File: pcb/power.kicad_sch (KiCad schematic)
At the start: 38 parts, among them Q1 AO3407A, Q2 PMV20EN, Q3 NCE3401AY, Q4 NCE3401AY, Q5 DMMT5401, U2 MT1471

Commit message: Basic value changes
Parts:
- R10, R11: value 220R -> 3k3
- R6: value 680R -> 510R
- R7: value 1.5k -> 10k; footprint Resistor_SMD:R_0805_2012Metric -> Resistor_SMD:R_0402_1005Metric
- R9: value 12k -> 39k
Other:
- note added: "EN threshold is 1.8V"
- note removed: "EN threshold is 0.8V"
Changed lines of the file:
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@@
     (stroke (width 0) (type default) (color 0 0 0 0))
   )
-  (text "EN threshold is 0.8V" (at 93.218 83.566 0)
+  (text "EN threshold is 1.8V" (at 93.218 83.566 0)
     (effects (font (size 1.27 1.27)) (justify left bottom))
   )
@@
       (effects (font (size 1.27 1.27)) (justify left))
     )
-    (property "Value" "1.5k" (id 1) (at 49.53 154.1779 0)
-      (effects (font (size 1.27 1.27)) (justify left))
-    )
-    (property "Footprint" "Resistor_SMD:R_0805_2012Metric" (id 2) (at 45.72 152.908 90)
+    (property "Value" "10k" (id 1) (at 49.53 154.1779 0)
+      (effects (font (size 1.27 1.27)) (justify left))
+    )
+    (property "Footprint" "Resistor_SMD:R_0402_1005Metric" (id 2) (at 45.72 152.908 90)
       (effects (font (size 1.27 1.27)) hide)
     )
@@
   (symbol (lib_id "Device:R") (at 94.615 160.655 0) (unit 1)
     (in_bom yes) (on_board yes) (fields_autoplaced)
-    (property "Reference" "R10" (id 0) (at 97.155 159.3849 0)
-      (effects (font (size 1.27 1.27)) (justify left))
-    )
-    (property "Value" "220R" (id 1) (at 97.155 161.9249 0)
+    (property "Reference" "R10" (id 0) (at 96.52 159.3849 0)
+      (effects (font (size 1.27 1.27)) (justify left))
+    )
+    (property "Value" "3k3" (id 1) (at 96.52 161.9249 0)
       (effects (font (size 1.27 1.27)) (justify left))
     )
@@
       (effects (font (size 1.27 1.27)) (justify left))
     )
-    (property "Value" "220R" (id 1) (at 121.92 161.9249 0)
+    (property "Value" "3k3" (id 1) (at 121.92 161.9249 0)
       (effects (font (size 1.27 1.27)) (justify left))
     )
@@
       (effects (font (size 1.27 1.27)) (justify left))
     )
-    (property "Value" "12k" (id 1) (at 91.44 80.0099 0)
+    (property "Value" "39k" (id 1) (at 91.44 80.0099 0)
       (effects (font (size 1.27 1.27)) (justify left))
     )
@@
       (effects (font (size 1.27 1.27)) hide)
     )
-    (pin "1")
-    (pin "2")
-    (pin "6")
     (pin "3")
     (pin "4")
@@
       (effects (font (size 1.27 1.27)) (justify right))
     )
-    (property "Value" "680R" (id 1) (at 138.43 88.8999 0)
+    (property "Value" "510R" (id 1) (at 138.43 88.8999 0)
       (effects (font (size 1.27 1.27)) (justify right))
     )
@@
     (pin "2")
     (pin "6")
-    (pin "3")
-    (pin "4")
-    (pin "5")
   )
   (symbol (lib_id "Device:C") (at 177.165 66.04 0) (unit 1)

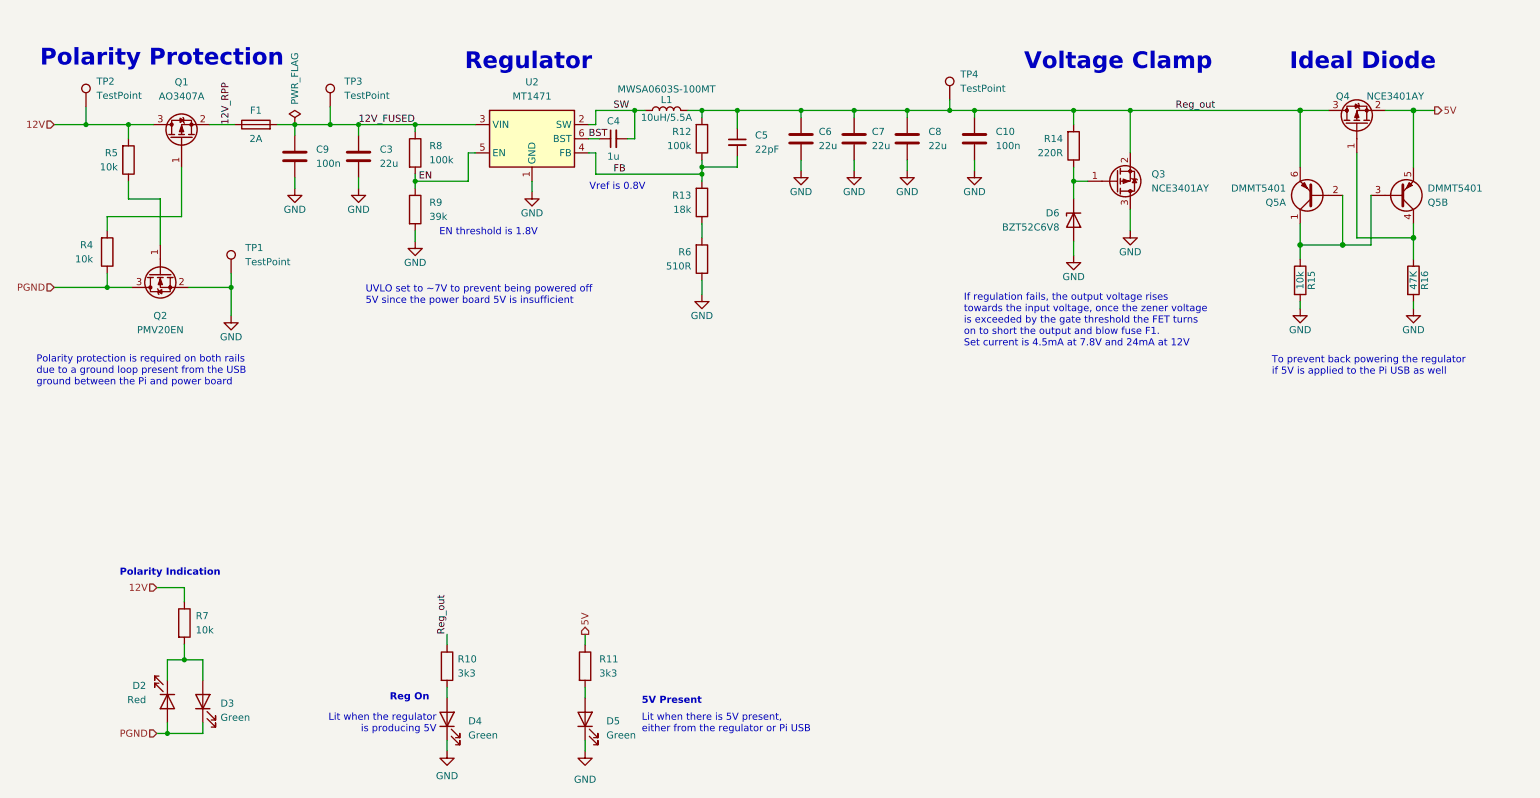
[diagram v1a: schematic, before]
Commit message: Update regulator to AP3200T
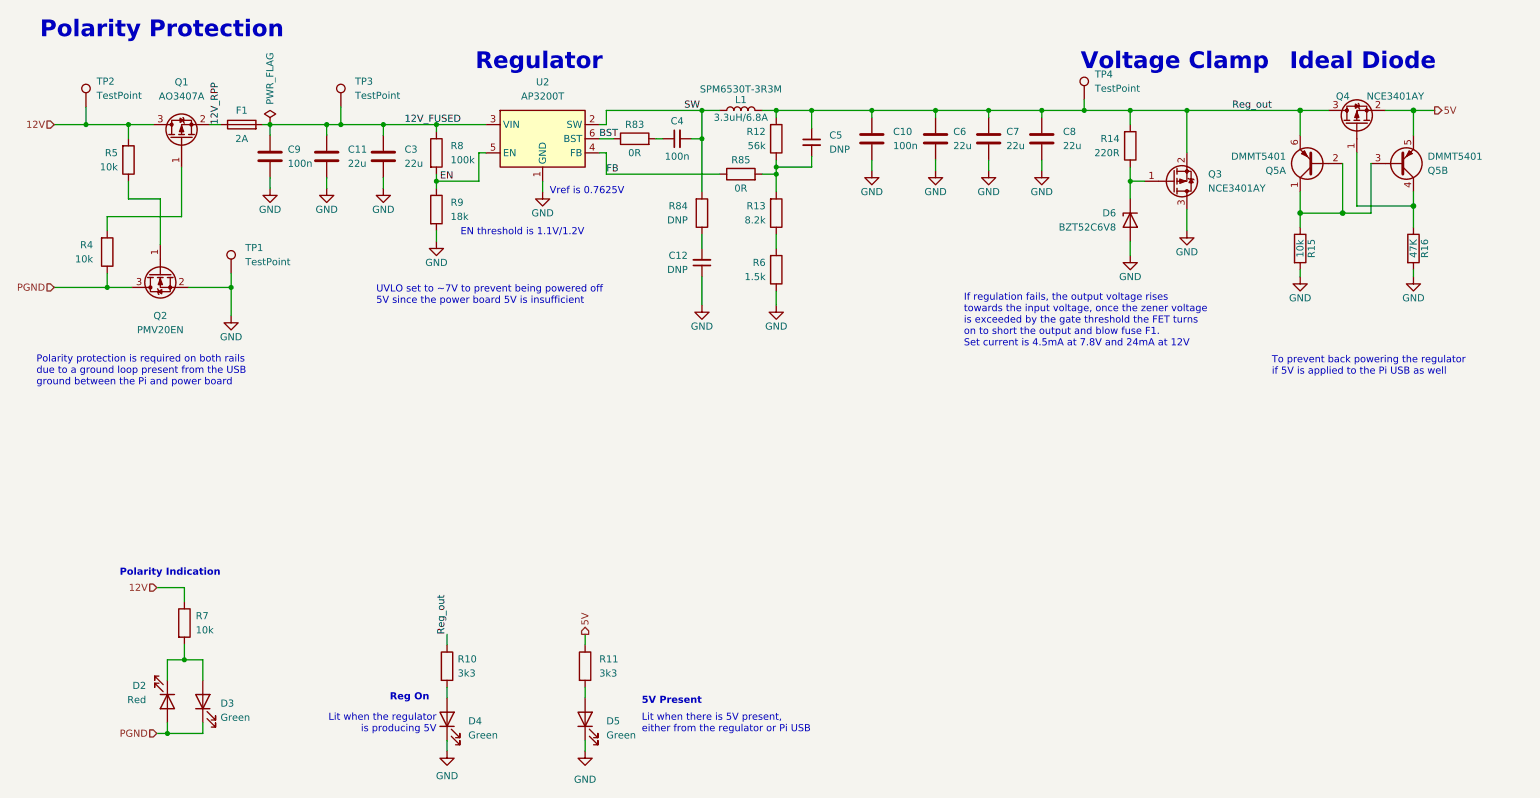
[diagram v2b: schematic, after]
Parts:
- added C11: 22u, Capacitor_SMD:C_1206_3216Metric, symbol Device:C
- added C12: DNP, Capacitor_SMD:C_0402_1005Metric, symbol Device:C_Small
- added R83, R85: 0R, Resistor_SMD:R_0402_1005Metric, symbol Device:R
- added R84: DNP, Resistor_SMD:R_0402_1005Metric, symbol Device:R
- C4: value 1u -> 100n
- C5: value 22pF -> DNP
- L1: value MWSA0603S-100MT -> SPM6530T-3R3M; Value2 10uH/5.5A -> 3.3uH/6.8A
- R12: value 100k -> 56k
- R13: value 18k -> 8.2k
- R6: value 510R -> 1.5k
- R9: value 39k -> 18k
- U2: value MT1471 -> AP3200T
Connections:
- net 12V_FUSED: now also C9.2, C11.1; no longer C9.1
- net BST: now also R83.1; no longer C4.1
- net FB: now also R85.1; no longer C5.2, R12.1, R13.2
- net GND: now also C9.1, C11.2, C12.1; no longer C9.2
- net SW: now also R84.2
- new net: C12.2, R84.1
- new net: C5.2, R12.1, R13.2, R85.2
- new net: C4.1, R83.2
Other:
- note added: "EN threshold is 1.1V/1.2V"
- note added: "Vref is 0.7625V"
- note removed: "EN threshold is 1.8V"
- note removed: "Vref is 0.8V"
- moved on the sheet: C10, C3, C4, C5, C6, C7, C8, C9, D6, F1, L1, Q3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

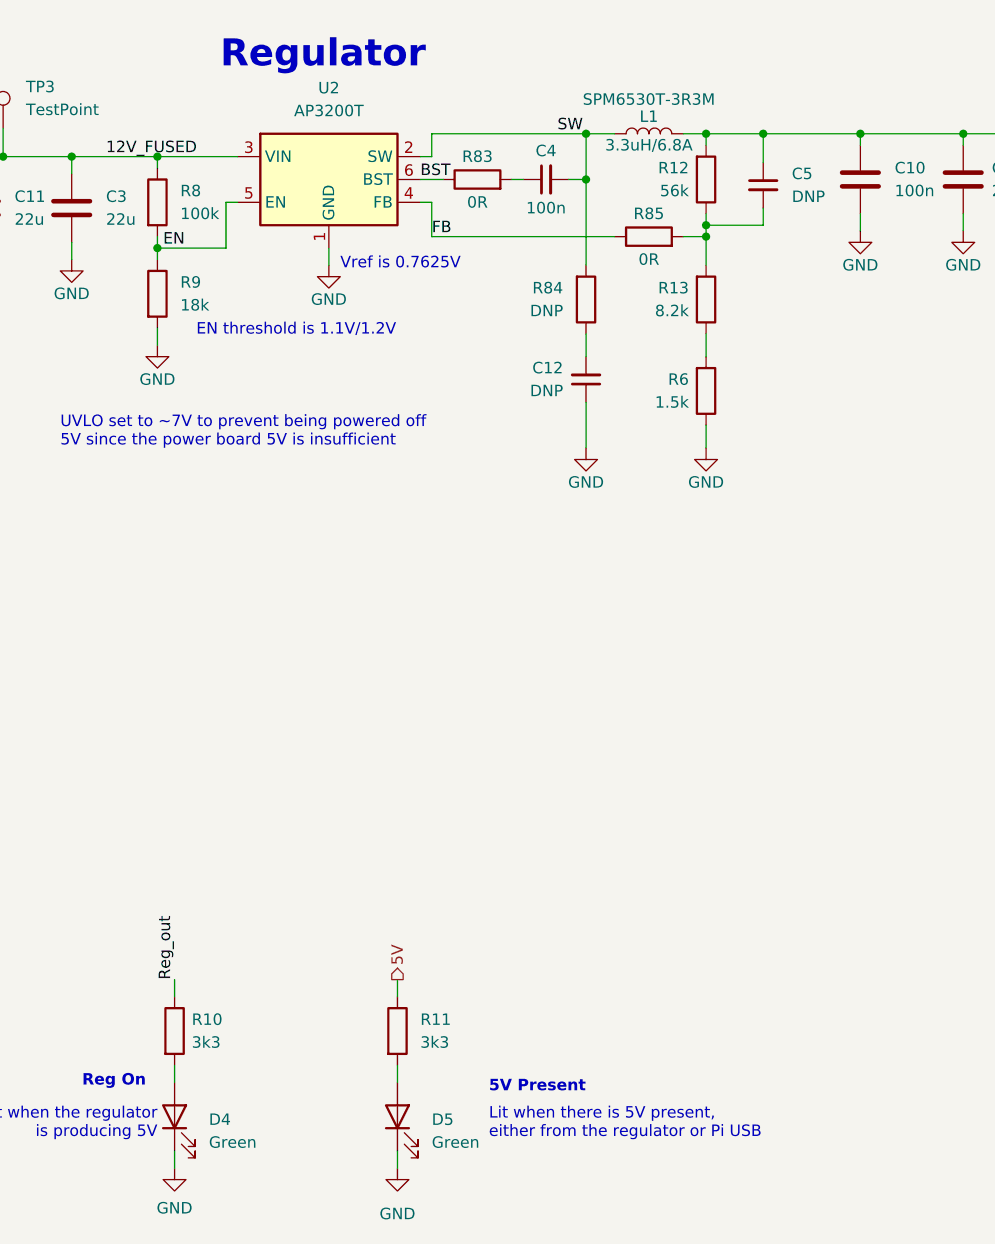
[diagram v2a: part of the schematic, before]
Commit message: Updated regulator layout
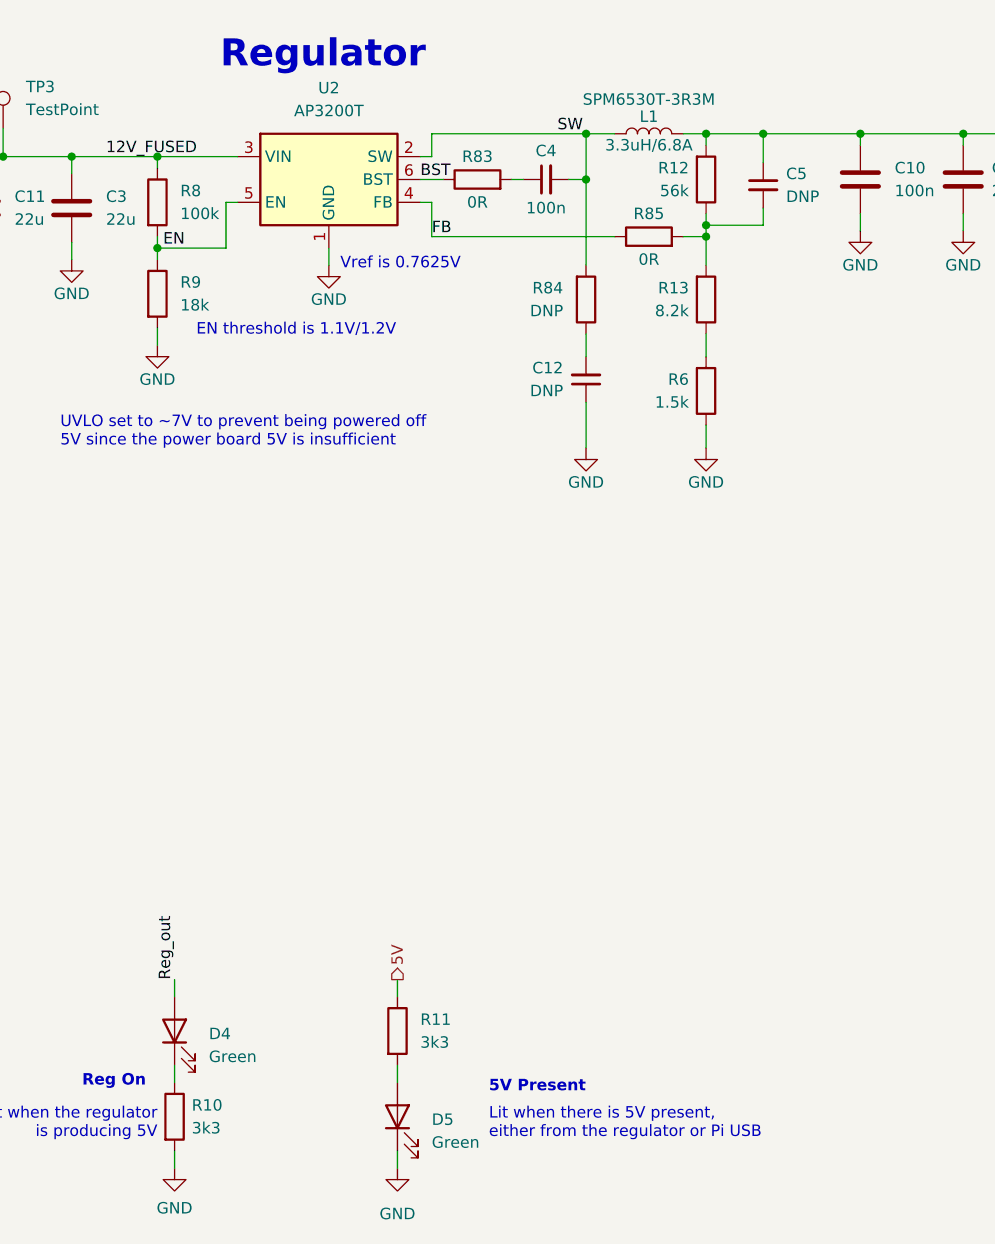
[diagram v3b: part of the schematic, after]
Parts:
- C5: footprint Capacitor_SMD:C_0603_1608Metric -> Capacitor_SMD:C_0402_1005Metric
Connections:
- net GND: now also R10.2; no longer D4.1 (K)
- net Reg_out: now also D4.2 (A); no longer R10.1
- new net: D4.1 (K), R10.1
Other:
- moved on the sheet: D4, R10
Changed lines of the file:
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@@
     (effects (font (size 1.27 1.27)) (justify right))
   )
-  (symbol (lib_id "Device:LED") (at 94.615 170.18 90) (unit 1)
-    (in_bom yes) (on_board yes) (fields_autoplaced)
-    (property "Reference" "D4" (id 0) (at 98.425 170.4974 90)
-      (effects (font (size 1.27 1.27)) (justify right))
-    )
-    (property "Value" "Green" (id 1) (at 98.425 173.0374 90)
-      (effects (font (size 1.27 1.27)) (justify right))
-    )
-    (property "Footprint" "LED_SMD:LED_0603_1608Metric_Pad1.05x0.95mm_HandSolder" (id 2) (at 94.615 170.18 0)
-      (effects (font (size 1.27 1.27)) hide)
-    )
-    (property "Datasheet" "https://datasheet.lcsc.com/lcsc/1811101510_Everlight-Elec-19-217-GHC-YR1S2-3T_C72043.pdf" (id 3) (at 94.615 170.18 0)
+  (symbol (lib_id "Device:LED") (at 94.615 160.655 90) (unit 1)
+    (in_bom yes) (on_board yes) (fields_autoplaced)
+    (property "Reference" "D4" (id 0) (at 98.425 160.9724 90)
+      (effects (font (size 1.27 1.27)) (justify right))
+    )
+    (property "Value" "Green" (id 1) (at 98.425 163.5124 90)
+      (effects (font (size 1.27 1.27)) (justify right))
+    )
+    (property "Footprint" "LED_SMD:LED_0603_1608Metric_Pad1.05x0.95mm_HandSolder" (id 2) (at 94.615 160.655 0)
+      (effects (font (size 1.27 1.27)) hide)
+    )
+    (property "Datasheet" "https://datasheet.lcsc.com/lcsc/1811101510_Everlight-Elec-19-217-GHC-YR1S2-3T_C72043.pdf" (id 3) (at 94.615 160.655 0)
       (effects (font (size 1.27 1.27)) hide)
     )
@@
     (pin "2")
   )
-  (symbol (lib_id "Device:R") (at 94.615 160.655 0) (unit 1)
-    (in_bom yes) (on_board yes) (fields_autoplaced)
-    (property "Reference" "R10" (id 0) (at 96.52 159.3849 0)
-      (effects (font (size 1.27 1.27)) (justify left))
-    )
-    (property "Value" "3k3" (id 1) (at 96.52 161.9249 0)
-      (effects (font (size 1.27 1.27)) (justify left))
-    )
-    (property "Footprint" "Resistor_SMD:R_0402_1005Metric" (id 2) (at 92.837 160.655 90)
-      (effects (font (size 1.27 1.27)) hide)
-    )
-    (property "Datasheet" "~" (id 3) (at 94.615 160.655 0)
+  (symbol (lib_id "Device:R") (at 94.615 170.18 0) (unit 1)
+    (in_bom yes) (on_board yes) (fields_autoplaced)
+    (property "Reference" "R10" (id 0) (at 96.52 168.9099 0)
+      (effects (font (size 1.27 1.27)) (justify left))
+    )
+    (property "Value" "3k3" (id 1) (at 96.52 171.4499 0)
+      (effects (font (size 1.27 1.27)) (justify left))
+    )
+    (property "Footprint" "Resistor_SMD:R_0402_1005Metric" (id 2) (at 92.837 170.18 90)
+      (effects (font (size 1.27 1.27)) hide)
+    )
+    (property "Datasheet" "~" (id 3) (at 94.615 170.18 0)
       (effects (font (size 1.27 1.27)) hide)
     )
@@
       (effects (font (size 1.27 1.27)) hide)
     )
-    (pin "1")
-    (pin "2")
-    (pin "6")
     (pin "3")
     (pin "4")
@@
   (symbol (lib_id "Device:C_Small") (at 160.02 66.675 0) (unit 1)
     (in_bom yes) (on_board yes) (fields_autoplaced)
-    (property "Reference" "C5" (id 0) (at 163.195 65.4112 0)
-      (effects (font (size 1.27 1.27)) (justify left))
-    )
-    (property "Value" "DNP" (id 1) (at 163.195 67.9512 0)
-      (effects (font (size 1.27 1.27)) (justify left))
-    )
-    (property "Footprint" "Capacitor_SMD:C_0603_1608Metric" (id 2) (at 160.02 66.675 0)
+    (property "Reference" "C5" (id 0) (at 162.56 65.4112 0)
+      (effects (font (size 1.27 1.27)) (justify left))
+    )
+    (property "Value" "DNP" (id 1) (at 162.56 67.9512 0)
+      (effects (font (size 1.27 1.27)) (justify left))
+    )
+    (property "Footprint" "Capacitor_SMD:C_0402_1005Metric" (id 2) (at 160.02 66.675 0)
       (effects (font (size 1.27 1.27)) hide)
     )
@@
     (pin "2")
     (pin "6")
-    (pin "3")
-    (pin "4")
-    (pin "5")
   )
   (symbol (lib_id "Device:C") (at 201.295 66.04 0) (unit 1)

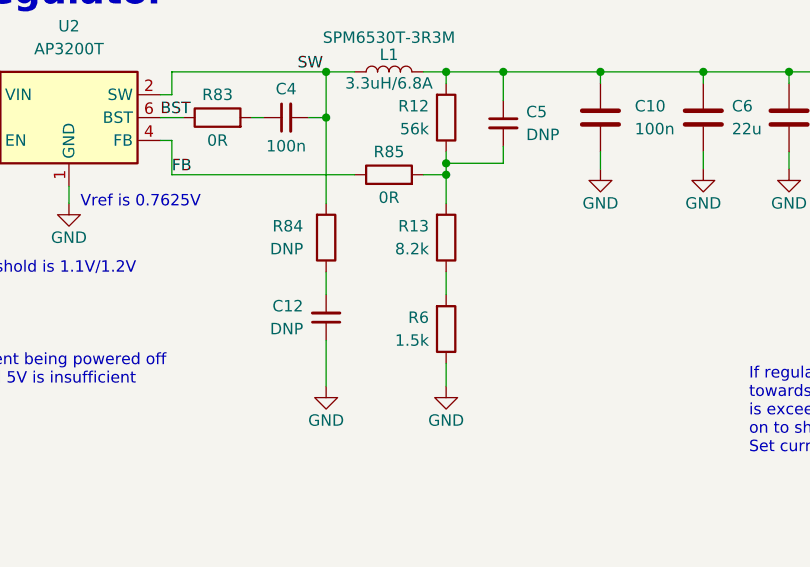
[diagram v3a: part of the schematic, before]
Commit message: Set JLCPCB parts
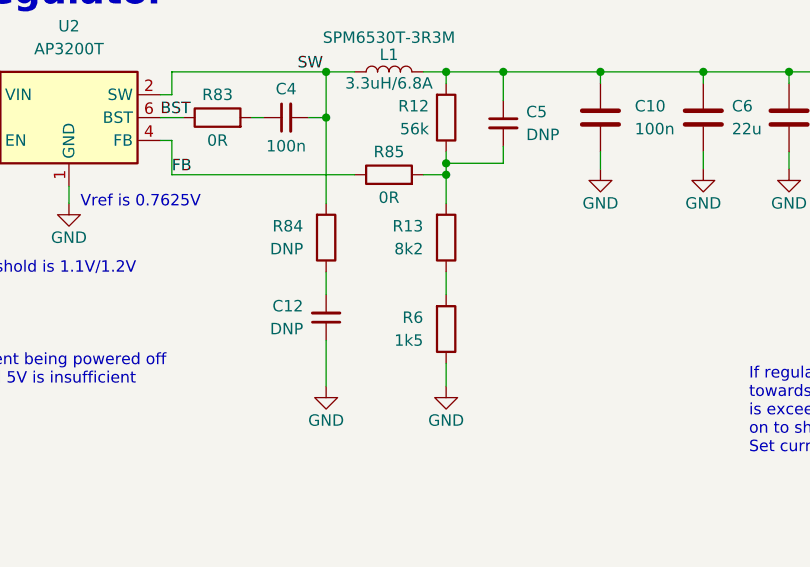
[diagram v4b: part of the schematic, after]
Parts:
- C12, C5, R84: now left out of the parts list
- C4: footprint Capacitor_SMD:C_0603_1608Metric -> Capacitor_SMD:C_0402_1005Metric
- R13: value 8.2k -> 8k2
- R6: value 1.5k -> 1k5
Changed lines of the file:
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@@
   )
   (symbol (lib_id "Device:C_Small") (at 140.335 88.265 0) (mirror x) (unit 1)
-    (in_bom yes) (on_board yes) (fields_autoplaced)
+    (in_bom no) (on_board yes) (fields_autoplaced)
     (property "Reference" "C12" (id 0) (at 137.795 86.9885 0)
       (effects (font (size 1.27 1.27)) (justify right))
@@
       (effects (font (size 1.27 1.27)) hide)
     )
+    (pin "1")
+    (pin "2")
+    (pin "6")
     (pin "3")
     (pin "4")
@@
   )
   (symbol (lib_id "Device:C_Small") (at 160.02 66.675 0) (unit 1)
-    (in_bom yes) (on_board yes) (fields_autoplaced)
+    (in_bom no) (on_board yes) (fields_autoplaced)
     (property "Reference" "C5" (id 0) (at 162.56 65.4112 0)
       (effects (font (size 1.27 1.27)) (justify left))
@@
   (symbol (lib_id "Device:R") (at 153.67 89.535 0) (mirror x) (unit 1)
     (in_bom yes) (on_board yes) (fields_autoplaced)
-    (property "Reference" "R6" (id 0) (at 151.765 88.2649 0)
-      (effects (font (size 1.27 1.27)) (justify right))
-    )
-    (property "Value" "1.5k" (id 1) (at 151.765 90.8049 0)
+    (property "Reference" "R6" (id 0) (at 151.13 88.2649 0)
+      (effects (font (size 1.27 1.27)) (justify right))
+    )
+    (property "Value" "1k5" (id 1) (at 151.13 90.8049 0)
       (effects (font (size 1.27 1.27)) (justify right))
     )
@@
   )
   (symbol (lib_id "Device:R") (at 140.335 79.375 0) (mirror x) (unit 1)
-    (in_bom yes) (on_board yes) (fields_autoplaced)
+    (in_bom no) (on_board yes) (fields_autoplaced)
     (property "Reference" "R84" (id 0) (at 137.795 78.1049 0)
       (effects (font (size 1.27 1.27)) (justify right))
@@
     (pin "2")
     (pin "6")
+    (pin "3")
+    (pin "4")
+    (pin "5")
   )
   (symbol (lib_id "Device:C") (at 201.295 66.04 0) (unit 1)
@@
   (symbol (lib_id "Device:R") (at 153.67 79.375 0) (mirror x) (unit 1)
     (in_bom yes) (on_board yes) (fields_autoplaced)
-    (property "Reference" "R13" (id 0) (at 151.765 78.1049 0)
-      (effects (font (size 1.27 1.27)) (justify right))
-    )
-    (property "Value" "8.2k" (id 1) (at 151.765 80.6449 0)
+    (property "Reference" "R13" (id 0) (at 151.13 78.1049 0)
+      (effects (font (size 1.27 1.27)) (justify right))
+    )
+    (property "Value" "8k2" (id 1) (at 151.13 80.6449 0)
       (effects (font (size 1.27 1.27)) (justify right))
     )
@@
     (property "Reference" "C4" (id 0) (at 135.89 62.865 90))
     (property "Value" "100n" (id 1) (at 135.89 69.215 90))
-    (property "Footprint" "Capacitor_SMD:C_0603_1608Metric" (id 2) (at 135.89 66.04 0)
-      (effects (font (size 1.27 1.27)) hide)
-    )
+    (property "Footprint" "Capacitor_SMD:C_0402_1005Metric" (id 2) (at 135.89 66.04 0)
+      (effects (font (size 1.27 1.27)) hide)
+    )
